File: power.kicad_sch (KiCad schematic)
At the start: 27 parts, among them U102 XC7A75T-1CSG324, U301 TPS82085, U302 TPS82085, U303 TPS82085, U304 TPS82085

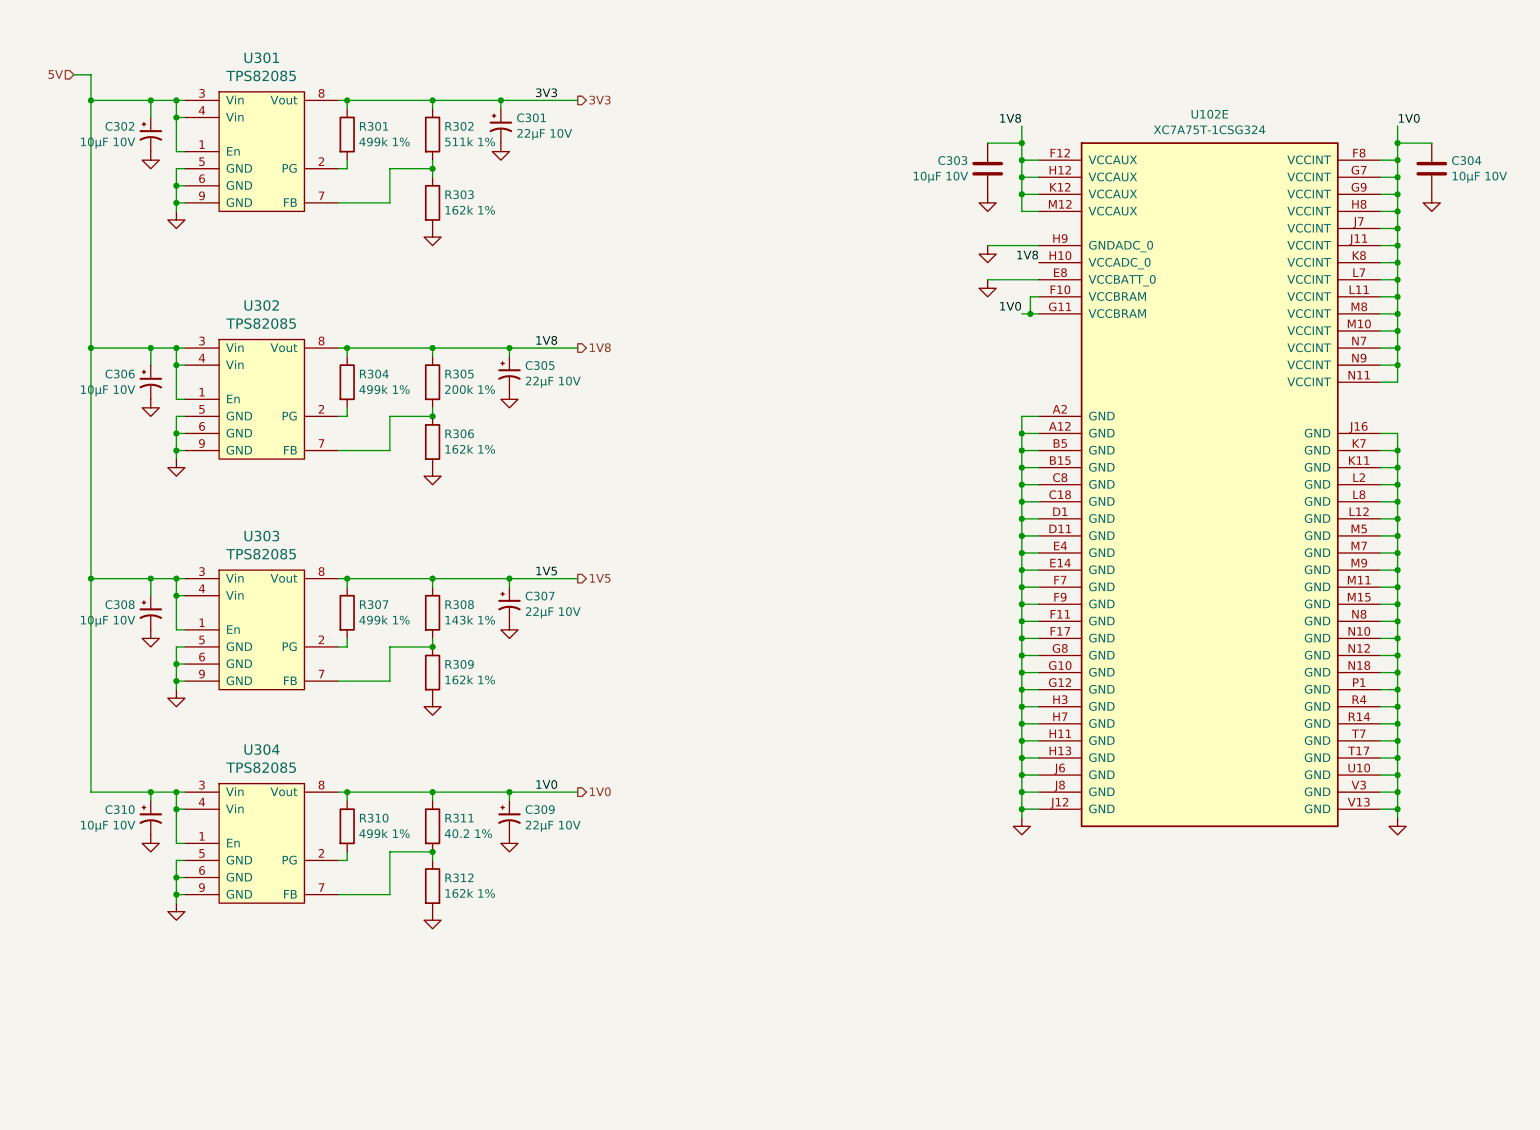
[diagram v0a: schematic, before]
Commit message: Cleaned up the directory and renamed files.  Also converted from the 324 package on the FPGA to the 484 package.  That conversion is still in-progress.
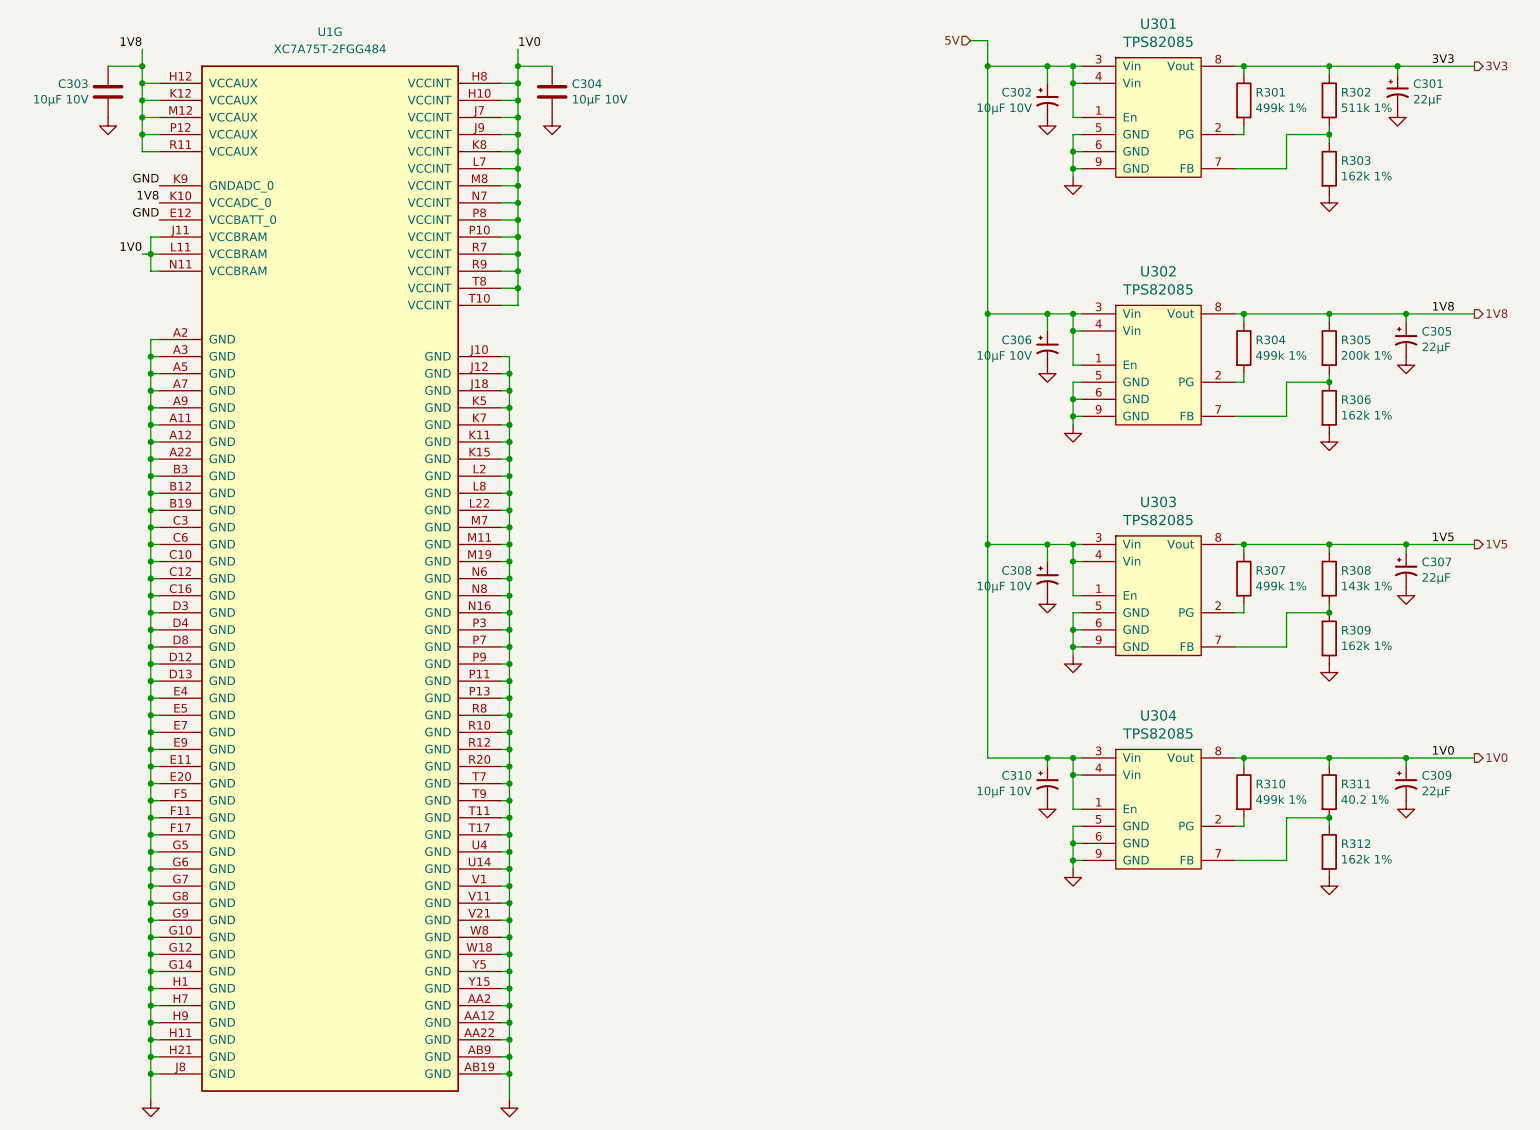
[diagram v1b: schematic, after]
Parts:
- removed U102: XC7A75T-1CSG324, Package_BGA:Xilinx_CSG324, symbol FPGA_Xilinx_Artix7:XC7A75T-CSG324
- added U1: XC7A75T-2FGG484, Package_BGA:Xilinx_FGG484, symbol FPGA_Xilinx_Artix7:XC7A75T-FGG484
- C301, C305, C307, C309: value 22µF 10V -> 22µF; JLCPCB Part (none) -> C59461
- C302, C303, C304, C306, C308, C310: JLCPCB Part (none) -> C85713
- R301, R304, R307, R310: JLCPCB Part (none) -> C131054
- R302: JLCPCB Part (none) -> C188257
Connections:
- net 1V0: now also U1.H10 (VCCINT), U1.H8 (VCCINT), U1.J11 (VCCBRAM), U1.J7 (VCCINT), U1.J9 (VCCINT), U1.K8 (VCCINT), U1.L11 (VCCBRAM), U1.L7 (VCCINT), U1.M8 (VCCINT), U1.N11 (VCCBRAM), U1.N7 (VCCINT), U1.P10 (VCCINT), U1.P8 (VCCINT), U1.R7 (VCCINT), U1.R9 (VCCINT), U1.T10 (VCCINT), U1.T8 (VCCINT)
- net 1V8: now also U1.H12 (VCCAUX), U1.K10 (VCCADC_0), U1.K12 (VCCAUX), U1.M12 (VCCAUX), U1.P12 (VCCAUX), U1.R11 (VCCAUX)
- net GND: now also U1.A11 (GND), U1.A12 (GND), U1.A2 (GND), U1.A22 (GND), U1.A3 (GND), U1.A5 (GND), U1.A7 (GND), U1.A9 (GND), U1.AA12 (GND), U1.AA2 (GND), U1.AA22 (GND), U1.AB19 (GND), U1.AB9 (GND), U1.B12 (GND), U1.B19 (GND), U1.B3 (GND), U1.C10 (GND), U1.C12 (GND), U1.C16 (GND), U1.C3 (GND), U1.C6 (GND), U1.D12 (GND), U1.D13 (GND), U1.D3 (GND), U1.D4 (GND), U1.D8 (GND), U1.E11 (GND), U1.E12 (VCCBATT_0), U1.E20 (GND), U1.E4 (GND), U1.E5 (GND), U1.E7 (GND), U1.E9 (GND), U1.F11 (GND), U1.F17 (GND), U1.F5 (GND), U1.G10 (GND), U1.G12 (GND), U1.G14 (GND), U1.G5 (GND), U1.G6 (GND), U1.G7 (GND), U1.G8 (GND), U1.G9 (GND), U1.H1 (GND), U1.H11 (GND), U1.H21 (GND), U1.H7 (GND), U1.H9 (GND), U1.J10 (GND), U1.J12 (GND), U1.J18 (GND), U1.J8 (GND), U1.K11 (GND), U1.K15 (GND), U1.K5 (GND), U1.K7 (GND), U1.K9 (GNDADC_0), U1.L2 (GND), U1.L22 (GND), U1.L8 (GND), U1.M11 (GND), U1.M19 (GND), U1.M7 (GND), U1.N16 (GND), U1.N6 (GND), U1.N8 (GND), U1.P11 (GND), U1.P13 (GND), U1.P3 (GND), U1.P7 (GND), U1.P9 (GND), U1.R10 (GND), U1.R12 (GND), U1.R20 (GND), U1.R8 (GND), U1.T11 (GND), U1.T17 (GND), U1.T7 (GND), U1.T9 (GND), U1.U14 (GND), U1.U4 (GND), U1.V1 (GND), U1.V11 (GND), U1.V21 (GND), U1.W18 (GND), U1.W8 (GND), U1.Y15 (GND), U1.Y5 (GND)
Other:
- moved on the sheet: C301, C302, C303, C304, C305, C306, C307, C308, C309, C310, R301, R302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

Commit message: Switched the level converters to 74HCT2G04 and 75LVC2G04.  Still need to remap the FPGA pins to the signal odering.
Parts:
- added C464, C465, C466, C467, C469, C470, C471, C472, C473, C474, C475, C476, C477, C478, C479, C480, C481, C482, C483, C484, C485, C486, C487, C488, C489, C490, C491, C492, C493, C494, C495, C496, C499, C500, C512, C513, C514, C515, C516, C517, C519: 100nF, Capacitor_SMD:C_0402_1005Metric, symbol Device:C
- added U10, U11, U12, U13, U14, U27, U3, U34, U38, U4, U40, U44, U46, U48, U5, U50, U52, U6, U7, U8, U9: 74LVC2GU04, Package_TO_SOT_SMD:SOT-363_SC-70-6, symbol 74xGxx:74LVC2GU04
- added U15, U16, U17, U18, U19, U20, U21, U22, U23, U24, U25, U26, U28, U29, U30, U32, U33, U35, U36, U41: 74HCT2GU04, Package_TO_SOT_SMD:SOT-363_SC-70-6, symbol 74xGxx:74LVC2GU04
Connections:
- net 3V3: now also C464.1, C465.1, C466.1, C467.1, C469.1, C470.1, C471.1, C472.1, C473.1, C474.1, C475.1, C476.1, C490.1, C492.1, C494.1, C496.1, C500.1, C513.1, C515.1, C517.1, C519.1, U10.5 (VCC), U11.5 (VCC), U12.5 (VCC), U13.5 (VCC), U14.5 (VCC), U27.5 (VCC), U3.5 (VCC), U34.5 (VCC), U38.5 (VCC), U4.5 (VCC), U40.5 (VCC), U44.5 (VCC), U46.5 (VCC), U48.5 (VCC), U5.5 (VCC), U50.5 (VCC), U52.5 (VCC), U6.5 (VCC), U7.5 (VCC), U8.5 (VCC), U9.5 (VCC)
- net 5V: now also C477.1, C478.1, C479.1, C480.1, C481.1, C482.1, C483.1, C484.1, C485.1, C486.1, C487.1, C488.1, C489.1, C491.1, C493.1, C495.1, C499.1, C512.1, C514.1, C516.1, U15.5 (VCC), U16.5 (VCC), U17.5 (VCC), U18.5 (VCC), U19.5 (VCC), U20.5 (VCC), U21.5 (VCC), U22.5 (VCC), U23.5 (VCC), U24.5 (VCC), U25.5 (VCC), U26.5 (VCC), U28.5 (VCC), U29.5 (VCC), U30.5 (VCC), U32.5 (VCC), U33.5 (VCC), U35.5 (VCC), U36.5 (VCC), U41.5 (VCC)
- net GND: now also C464.2, C465.2, C466.2, C467.2, C469.2, C470.2, C471.2, C472.2, C473.2, C474.2, C475.2, C476.2, C477.2, C478.2, C479.2, C480.2, C481.2, C482.2, C483.2, C484.2, C485.2, C486.2, C487.2, C488.2, C489.2, C490.2, C491.2, C492.2, C493.2, C494.2, C495.2, C496.2, C499.2, C500.2, C512.2, C513.2, C514.2, C515.2, C516.2, C517.2, C519.2, U10.2 (GND), U11.2 (GND), U12.2 (GND), U13.2 (GND), U14.2 (GND), U15.2 (GND), U16.2 (GND), U17.2 (GND), U18.2 (GND), U19.2 (GND), U20.2 (GND), U21.2 (GND), U22.2 (GND), U23.2 (GND), U24.2 (GND), U25.2 (GND), U26.2 (GND), U27.2 (GND), U28.2 (GND), U29.2 (GND), U3.2 (GND), U30.2 (GND), U32.2 (GND), U33.2 (GND), U34.2 (GND), U35.2 (GND), U36.2 (GND), U38.2 (GND), U4.2 (GND), U40.2 (GND), U41.2 (GND), U44.2 (GND), U46.2 (GND), U48.2 (GND), U5.2 (GND), U50.2 (GND), U52.2 (GND), U6.2 (GND), U7.2 (GND), U8.2 (GND), U9.2 (GND)
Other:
- note added: "QBUS Driver Level Converters"
- company: (none) -> Vintage Computer Enterprises
- moved on the sheet: C301, C302, C303, C304, C305, C306, C307, C308, C309, C310, R301, R302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
